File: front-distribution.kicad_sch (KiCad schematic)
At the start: 84 parts, among them J1 USB_C_Receptacle_USB2.0_14P, J2 Conn_01x23, J3 Conn_01x06, J8 Conn_01x35, J9 Conn_01x08, Q1 AO3400A, Q3 AO3400A, Q4 AO3400A, SW1 SW_Push, U1 TPS7B88, U2 MCP1700x-330xxMB, U3 MAX3232CDR, U4 USBLC6-2SC6, U5 STM32F103C8Tx, U6 SN65HVD1050D, U7 M24C64-R, Y1 8M

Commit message: Updated revision variable
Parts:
- JP1: footprint (none) -> Jumper:SolderJumper-2_P1.3mm_Open_RoundedPad1.0x1.5mm
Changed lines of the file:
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@@
 			)
 		)
-		(property "Footprint" ""
+		(property "Footprint" "Jumper:SolderJumper-2_P1.3mm_Open_RoundedPad1.0x1.5mm"
 			(at 101.6 73.66 0)
 			(effects

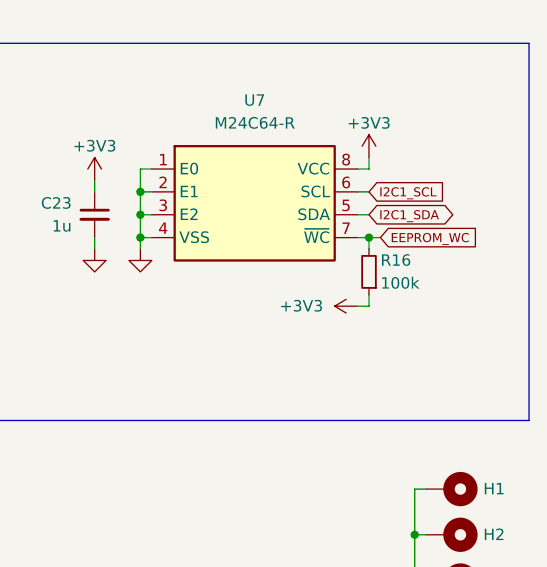
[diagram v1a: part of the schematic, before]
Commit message: Updated CAN termination resistors
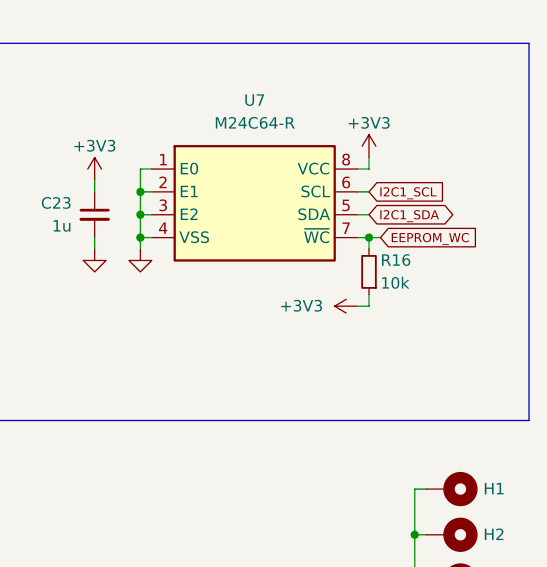
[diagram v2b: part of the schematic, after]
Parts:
- R12, R7: footprint Resistor_SMD:R_2512_6332Metric -> Resistor_SMD:R_1206_3216Metric
- R16: value 100k -> 10k
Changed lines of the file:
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@@
 			)
 		)
-		(property "Footprint" "Resistor_SMD:R_2512_6332Metric"
+		(property "Footprint" "Resistor_SMD:R_1206_3216Metric"
 			(at 119.38 122.682 90)
 			(effects
@@
 			)
 		)
-		(property "Value" "100k"
+		(property "Value" "10k"
 			(at 388.62 207.01 0)
 			(effects
@@
 			)
 		)
-		(property "Footprint" "Resistor_SMD:R_2512_6332Metric"
+		(property "Footprint" "Resistor_SMD:R_1206_3216Metric"
 			(at 119.38 117.602 90)
 			(effects
